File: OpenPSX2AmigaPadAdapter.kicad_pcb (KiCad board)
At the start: 2 copper layers, 58.9 x 44.2 mm, 39 parts, among them J1 TO_PSX_PAD, J2 DB9_F, J3 CONN_FTDI, J4 CONN_ICSP, J99 OSHW_LOGO, Q1 BSS138, Q2 BSS138, Q3 BSS138, Q4 BSS138, SW1 RESET, U1 ATmega328P-AU, U2 LM1117-3.3, Y1 16M, Y2 16M

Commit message: Cosmetic fixes
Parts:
- moved R13 1.98 mm to (120.5, 63.0)
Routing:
- net +3V3: track 63.5 -> 61.6 mm
- net /ps_ack_3v3: track 3.85 -> 5.40 mm
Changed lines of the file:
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@@
     (thickness 1.6)
     (drawings 27)
-    (tracks 352)
+    (tracks 354)
     (zones 0)
     (modules 39)
@@
     (tags "Diode SMA (DO-214AC)")
     (attr smd)
-    (fp_text reference D1 (at -4.445 0 180) (layer F.SilkS)
+    (fp_text reference D1 (at 4.445 0 180) (layer F.SilkS)
       (effects (font (size 1 1) (thickness 0.15)))
     )
@@
   )
   (module Resistor_SMD:R_0805_2012Metric_Pad1.15x1.40mm_HandSolder (layer F.Cu)
-    (at 120.4645 61.0075 90)
+    (at 120.4645 62.992 90)
     (descr "Resistor SMD 0805 (2012 Metric), square (rectangular) end terminal, IPC_7351 nominal with elongated pad for handsoldering. (Body size source: https://docs.google.com/spreadsheets/d/1BsfQQcO9C6DZCsRaXUlFlo91Tg2WpOkGARC1WS5S8t0/edit?usp=sharing), generated with kicad-footprint-generator")
     (tags "resistor handsolder")
     (attr smd)
-    (fp_text reference R13 (at -2.6195 0 180) (layer F.SilkS)
+    (fp_text reference R13 (at 2.921 0 180) (layer F.SilkS)
       (effects (font (size 1 1) (thickness 0.15)))
     )
@@
     (tags "resistor handsolder")
     (attr smd)
-    (fp_text reference R14 (at 2.54 -0.0585 180) (layer F.SilkS)
+    (fp_text reference R14 (at -3.175 -0.0585 180) (layer F.SilkS)
       (effects (font (size 1 1) (thickness 0.15)))
     )
@@
   (segment (start 120.888764 75.9825) (end 124.206 75.9825) (width 0.25) (layer B.Cu) (net 3))
   (segment (start 120.4645 75.9825) (end 120.888764 75.9825) (width 0.25) (layer B.Cu) (net 3))
-  (segment (start 120.4645 65.668) (end 120.4645 62.0325) (width 0.25) (layer F.Cu) (net 3))
   (segment (start 120.4645 81.162) (end 120.4645 82.414) (width 0.25) (layer F.Cu) (net 3))
+  (segment (start 120.4645 64.017) (end 120.4645 65.668) (width 0.25) (layer F.Cu) (net 3))
   (segment (start 141.187 85.598) (end 141.187 89.916) (width 0.25) (layer F.Cu) (net 4))
   (segment (start 142.457 84.328) (end 141.187 85.598) (width 0.25) (layer F.Cu) (net 4))
@@
   (segment (start 119.32725 90.37125) (end 119.32725 80.82475) (width 0.25) (layer B.Cu) (net 9))
   (segment (start 116.616 91.9825) (end 117.716 91.9825) (width 0.25) (layer B.Cu) (net 9))
-  (segment (start 120.4645 84.464) (end 120.4645 91.4985) (width 0.25) (layer F.Cu) (net 9))
-  (segment (start 119.9805 91.9825) (end 116.616 91.9825) (width 0.25) (layer F.Cu) (net 9))
-  (segment (start 120.4645 91.4985) (end 119.9805 91.9825) (width 0.25) (layer F.Cu) (net 9))
+  (segment (start 120.4645 91.3815) (end 120.4645 84.464) (width 0.25) (layer F.Cu) (net 9))
+  (segment (start 119.8635 91.9825) (end 120.4645 91.3815) (width 0.25) (layer F.Cu) (net 9))
+  (segment (start 116.616 91.9825) (end 119.8635 91.9825) (width 0.25) (layer F.Cu) (net 9))
   (segment (start 124.281 74.022332) (end 124.206 73.947332) (width 0.25) (layer B.Cu) (net 10))
   (segment (start 124.281 74.0075) (end 124.206 73.9325) (width 0.25) (layer B.Cu) (net 10))
@@
   (segment (start 146.059 68.834) (end 149.089 68.834) (width 0.25) (layer F.Cu) (net 29))
   (segment (start 146.059 65.024) (end 149.089 65.024) (width 0.25) (layer F.Cu) (net 30))
-  (segment (start 116.616 59.9825) (end 120.4645 59.9825) (width 0.25) (layer F.Cu) (net 31))
+  (segment (start 120.4645 60.7245) (end 119.7225 59.9825) (width 0.25) (layer F.Cu) (net 31))
+  (segment (start 120.4645 61.967) (end 120.4645 60.7245) (width 0.25) (layer F.Cu) (net 31))
+  (segment (start 116.616 59.9825) (end 119.7225 59.9825) (width 0.25) (layer F.Cu) (net 31))
   (zone (net 1) (net_name GND) (layer F.Cu) (hatch edge 0.508)
     (connect_pads (clearance 0.1))

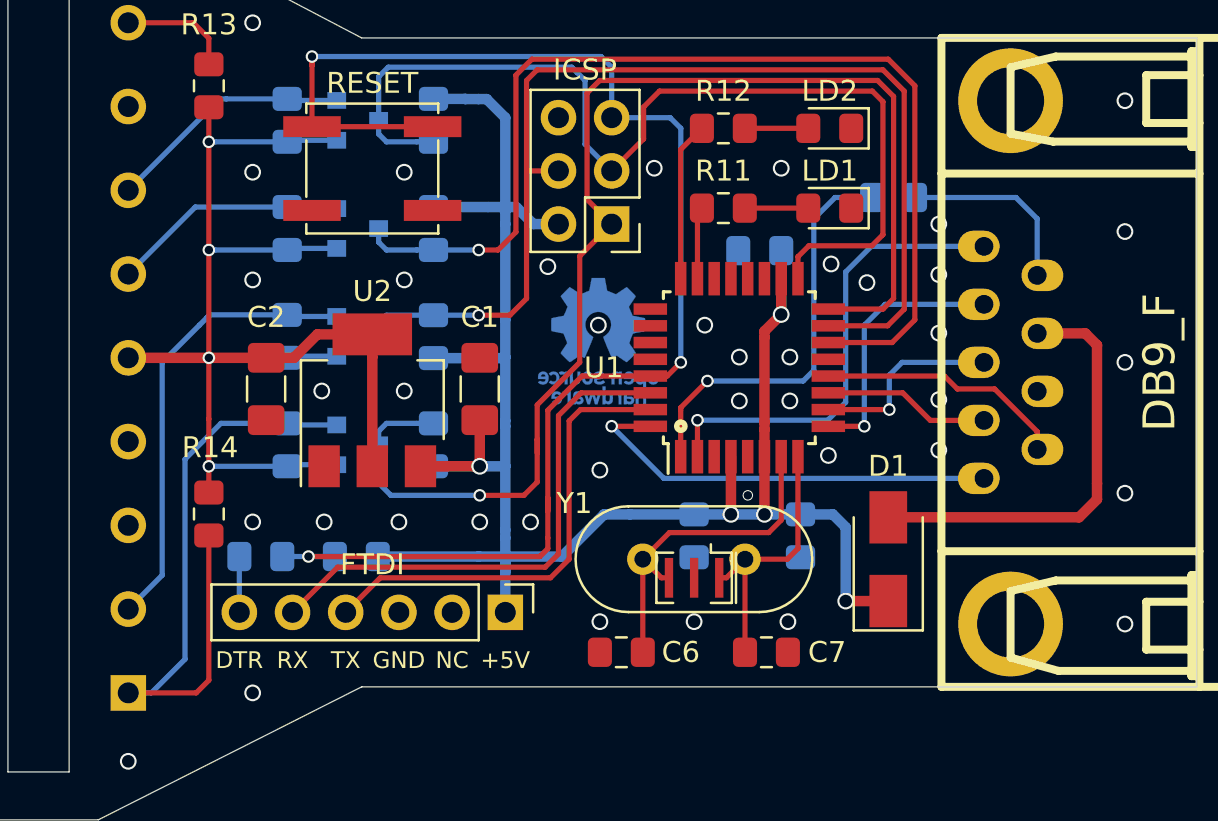
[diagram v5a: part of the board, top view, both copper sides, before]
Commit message: Update PCB after changes to schematics
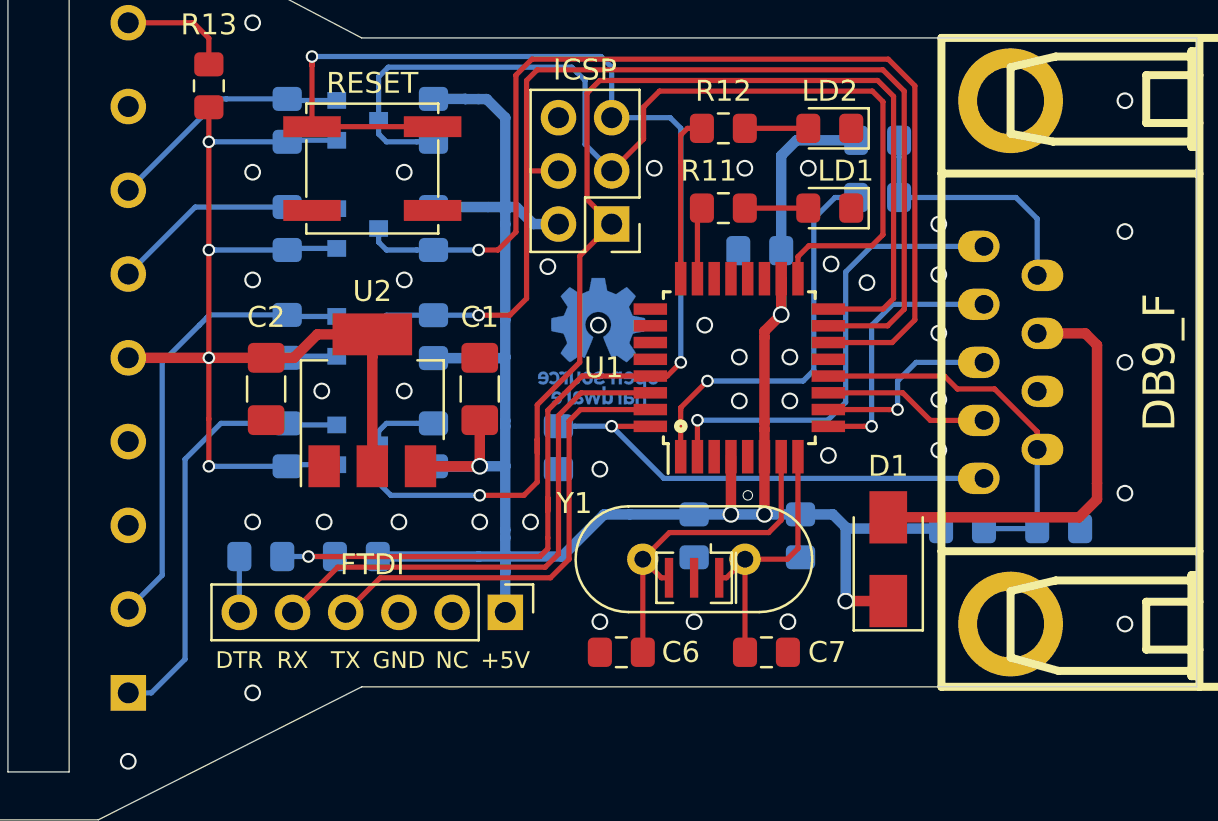
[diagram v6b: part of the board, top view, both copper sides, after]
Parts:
- added C10: 220p, Capacitor_SMD:C_0805_2012Metric_Pad1.15x1.40mm_HandSolder, B.Cu at (137.2, 80.3)
- added C9: 820p, Capacitor_SMD:C_0805_2012Metric_Pad1.15x1.40mm_HandSolder, B.Cu at (161.0, 84.1)
- added R15: 10k, Resistor_SMD:R_0805_2012Metric_Pad1.15x1.40mm_HandSolder, B.Cu at (152.4, 65.6)
- R14: moved to B.Cu
- moved R14 36.0 mm to (156.5, 84.1), turned to 0 degrees
- moved R10 0.76 mm to (152.4, 68.3)
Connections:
- R14 pad 1: +3V3 -> +5V
- R14 pad 2: /ps_data_3v3 -> /ami_poty
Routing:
- net +5V: track 92.9 -> 106.0 mm
- net /ps_data_3v3: track 31.9 -> 20.9 mm
- net /ami_poty: track 11.9 -> 18.2 mm
- net /ami_fire: track 8.96 -> 12.4 mm
- net /ami_potx: track 20.7 -> 23.2 mm
- net +3V3: track 61.6 -> 60.3 mm
- net Net-(R10-Pad2): track 19.9 -> 19.0 mm
- net GND: vias 42 -> 43
